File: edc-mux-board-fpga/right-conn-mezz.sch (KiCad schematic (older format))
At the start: 86 parts, among them J21 Device 10, J22 Device 13, J23 Device 11, J24 Device 14, J25 Left Mezzanine Board Connecto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, J26 Left Mezzanine Board Connecto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, J27 Device 12, J28 Device 15

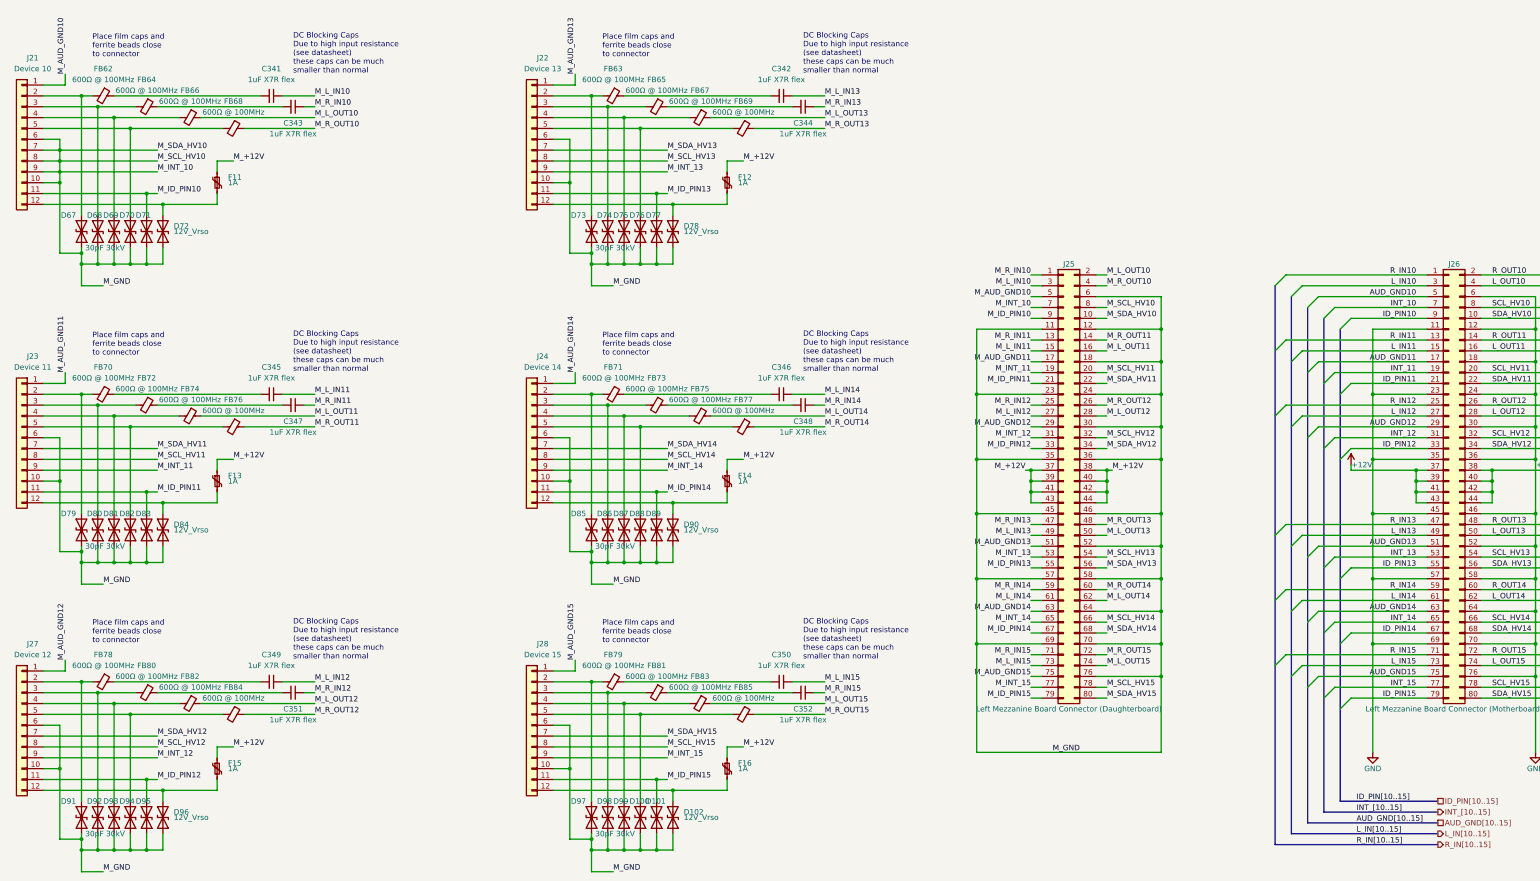
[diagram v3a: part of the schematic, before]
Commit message: re-annotating after adding power ICs and decoupling capacitors.
Also verified most footprints, and updated schematic field data.
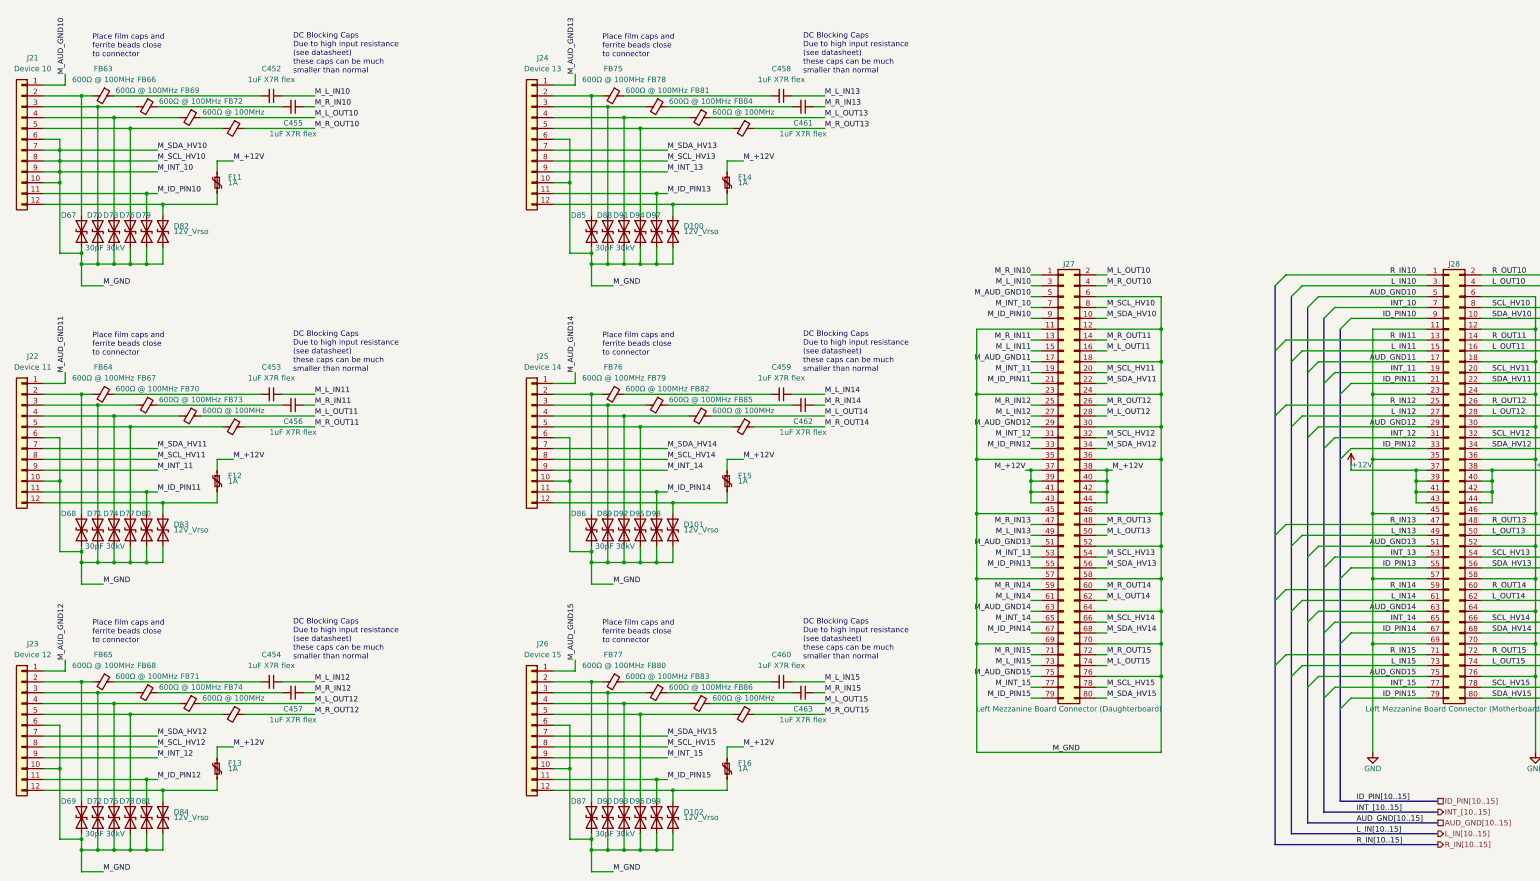
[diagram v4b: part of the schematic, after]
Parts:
- renumbered C341 to C452, C345 to C453, C349 to C454, C343 to C455, C347 to C456, C351 to C457, C342 to C458, C346 to C459, C350 to C460, C344 to C461, C348 to C462, C352 to C463, D78 to D100, D90 to D101, D79 to D68, D91 to D69, D68 to D70, D80 to D71, D92 to D72, D69 to D73, D81 to D74, D93 to D75, D70 to D76, D82 to D77, D94 to D78, D71 to D79, D83 to D80, D95 to D81, D72 to D82, D84 to D83, D96 to D84, D73 to D85, D85 to D86, D97 to D87, D74 to D88, D86 to D89, D98 to D90, D75 to D91, D87 to D92, D99 to D93, D76 to D94, D88 to D95, D100 to D96, D77 to D97, D89 to D98, D101 to D99, F13 to F12, F15 to F13, F12 to F14, F14 to F15, FB62 to FB63, FB70 to FB64, FB78 to FB65, FB64 to FB66, FB72 to FB67, FB80 to FB68, FB66 to FB69, FB74 to FB70, FB82 to FB71, FB68 to FB72, FB76 to FB73, FB84 to FB74, FB63 to FB75, FB71 to FB76, FB79 to FB77, FB65 to FB78, FB73 to FB79, FB81 to FB80, FB67 to FB81, FB75 to FB82, FB69 to FB84, FB77 to FB85, FB85 to FB86, J23 to J22, J27 to J23, J22 to J24, J24 to J25, J28 to J26, J25 to J27, J26 to J28

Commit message: removed polyfuses
at the right rating they were going to be too big.
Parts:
- removed F11, F12, F13, F14, F15, F16: 1A, Fuse:Fuse_0603_1608Metric, symbol Device:Polyfuse_Small
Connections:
- net M_+12V: now also D100.1 (A1), D101.1 (A1), D102.1 (A1), D82.1 (A1), D83.1 (A1), D84.1 (A1), J21.12 (Pin_12), J22.12 (Pin_12), J23.12 (Pin_12), J24.12 (Pin_12), J25.12 (Pin_12), J26.12 (Pin_12)
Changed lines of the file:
@@
 Wire Wire Line
 	1000 2600 2100 2600
-Wire Wire Line
-	2600 2600 2600 2500
 Text Label 2050 2100 0    50   ~ 0
 M_SDA_HV10
@@
 Text Label 2050 2500 0    50   ~ 0
 M_ID_PIN10
-$Comp
-L Device:Polyfuse_Small F?
-U 1 1 61B47DFE
-P 2600 2400
-AR Path="/5CC6CC1A/5CC6D47B/61B47DFE" Ref="F?"  Part="1"
-AR Path="/5CB02488/61B47DFE" Ref="F?"  Part="1"
-AR Path="/5CBF625C/61B47DFE" Ref="F?"  Part="1"
-AR Path="/5CBF628A/61B47DFE" Ref="F11"  Part="1"
-F 0 "F11" H 2700 2450 50  0000 L CNN
-F 1 "1A" H 2700 2400 50  0000 L CNN
-F 2 "Fuse:Fuse_0603_1608Metric" H 2650 2200 50  0001 L CNN
-F 3 "~" H 2600 2400 50  0001 C CNN
-F 4 "0603in/1608mm" H 400 -1600 50  0001 C CNN "Package ID"
-	1    2600 2400
-	1    0    0    -1
-$EndComp
 Wire Wire Line
 	2100 2600 2600 2600
-Wire Wire Line
-	2600 2300 2600 2200
 Text Label 1550 3350 0    50   ~ 0
 M_GND
@@
 Wire Wire Line
 	1000 5350 2100 5350
-Wire Wire Line
-	2600 5350 2600 5250
 Text Label 2050 4850 0    50   ~ 0
 M_SDA_HV11
@@
 Text Label 2050 5250 0    50   ~ 0
 M_ID_PIN11
-$Comp
-L Device:Polyfuse_Small F?
-U 1 1 61B47EDE
-P 2600 5150
-AR Path="/5CC6CC1A/5CC6D47B/61B47EDE" Ref="F?"  Part="1"
-AR Path="/5CB02488/61B47EDE" Ref="F?"  Part="1"
-AR Path="/5CBF625C/61B47EDE" Ref="F?"  Part="1"
-AR Path="/5CBF628A/61B47EDE" Ref="F12"  Part="1"
-F 0 "F12" H 2700 5200 50  0000 L CNN
-F 1 "1A" H 2700 5150 50  0000 L CNN
-F 2 "Fuse:Fuse_0603_1608Metric" H 2650 4950 50  0001 L CNN
-F 3 "~" H 2600 5150 50  0001 C CNN
-F 4 "0603in/1608mm" H 400 1150 50  0001 C CNN "Package ID"
-	1    2600 5150
-	1    0    0    -1
-$EndComp
 Wire Wire Line
 	2100 5350 2600 5350
-Wire Wire Line
-	2600 5050 2600 4950
 Text Label 1550 6100 0    50   ~ 0
 M_GND
@@
 Wire Wire Line
 	1000 8000 2100 8000
-Wire Wire Line
-	2600 8000 2600 7900
 Text Label 2050 7500 0    50   ~ 0
 M_SDA_HV12
@@
 Text Label 2050 7900 0    50   ~ 0
 M_ID_PIN12
-$Comp
-L Device:Polyfuse_Small F?
-U 1 1 61B47FAF
-P 2600 7800
-AR Path="/5CC6CC1A/5CC6D47B/61B47FAF" Ref="F?"  Part="1"
-AR Path="/5CB02488/61B47FAF" Ref="F?"  Part="1"
-AR Path="/5CBF625C/61B47FAF" Ref="F?"  Part="1"
-AR Path="/5CBF628A/61B47FAF" Ref="F13"  Part="1"
-F 0 "F13" H 2700 7850 50  0000 L CNN
-F 1 "1A" H 2700 7800 50  0000 L CNN
-F 2 "Fuse:Fuse_0603_1608Metric" H 2650 7600 50  0001 L CNN
-F 3 "~" H 2600 7800 50  0001 C CNN
-F 4 "0603in/1608mm" H 400 3800 50  0001 C CNN "Package ID"
-	1    2600 7800
-	1    0    0    -1
-$EndComp
 Wire Wire Line
 	2100 8000 2600 8000
-Wire Wire Line
-	2600 7700 2600 7600
 Text Label 1550 8750 0    50   ~ 0
 M_GND
@@
 Wire Wire Line
 	5700 2600 6800 2600
-Wire Wire Line
-	7300 2600 7300 2500
 Text Label 6750 2100 0    50   ~ 0
 M_SDA_HV13
@@
 Text Label 6750 2500 0    50   ~ 0
 M_ID_PIN13
-$Comp
-L Device:Polyfuse_Small F?
-U 1 1 61B48080
-P 7300 2400
-AR Path="/5CC6CC1A/5CC6D47B/61B48080" Ref="F?"  Part="1"
-AR Path="/5CB02488/61B48080" Ref="F?"  Part="1"
-AR Path="/5CBF625C/61B48080" Ref="F?"  Part="1"
-AR Path="/5CBF628A/61B48080" Ref="F14"  Part="1"
-F 0 "F14" H 7400 2450 50  0000 L CNN
-F 1 "1A" H 7400 2400 50  0000 L CNN
-F 2 "Fuse:Fuse_0603_1608Metric" H 7350 2200 50  0001 L CNN
-F 3 "~" H 7300 2400 50  0001 C CNN
-F 4 "0603in/1608mm" H 5100 -1600 50  0001 C CNN "Package ID"
-	1    7300 2400
-	1    0    0    -1
-$EndComp
 Wire Wire Line
 	6800 2600 7300 2600
-Wire Wire Line
-	7300 2300 7300 2200
 Text Label 6250 3350 0    50   ~ 0
 M_GND
@@
 Wire Wire Line
 	5700 5350 6800 5350
-Wire Wire Line
-	7300 5350 7300 5250
 Text Label 6750 4850 0    50   ~ 0
 M_SDA_HV14
@@
 Text Label 6750 5250 0    50   ~ 0
 M_ID_PIN14
-$Comp
-L Device:Polyfuse_Small F?
-U 1 1 61B48151
-P 7300 5150
-AR Path="/5CC6CC1A/5CC6D47B/61B48151" Ref="F?"  Part="1"
-AR Path="/5CB02488/61B48151" Ref="F?"  Part="1"
-AR Path="/5CBF625C/61B48151" Ref="F?"  Part="1"
-AR Path="/5CBF628A/61B48151" Ref="F15"  Part="1"
-F 0 "F15" H 7400 5200 50  0000 L CNN
-F 1 "1A" H 7400 5150 50  0000 L CNN
-F 2 "Fuse:Fuse_0603_1608Metric" H 7350 4950 50  0001 L CNN
-F 3 "~" H 7300 5150 50  0001 C CNN
-F 4 "0603in/1608mm" H 5100 1150 50  0001 C CNN "Package ID"
-	1    7300 5150
-	1    0    0    -1
-$EndComp
 Wire Wire Line
 	6800 5350 7300 5350
-Wire Wire Line
-	7300 5050 7300 4950
 Text Label 6250 6100 0    50   ~ 0
 M_GND
@@
 Wire Wire Line
 	5700 8000 6800 8000
-Wire Wire Line
-	7300 8000 7300 7900
 Text Label 6750 7500 0    50   ~ 0
 M_SDA_HV15
@@
 Text Label 6750 7900 0    50   ~ 0
 M_ID_PIN15
-$Comp
-L Device:Polyfuse_Small F?
-U 1 1 61B48222
-P 7300 7800
-AR Path="/5CC6CC1A/5CC6D47B/61B48222" Ref="F?"  Part="1"
-AR Path="/5CB02488/61B48222" Ref="F?"  Part="1"
-AR Path="/5CBF625C/61B48222" Ref="F?"  Part="1"
-AR Path="/5CBF628A/61B48222" Ref="F16"  Part="1"
-F 0 "F16" H 7400 7850 50  0000 L CNN
-F 1 "1A" H 7400 7800 50  0000 L CNN
-F 2 "Fuse:Fuse_0603_1608Metric" H 7350 7600 50  0001 L CNN
-F 3 "~" H 7300 7800 50  0001 C CNN
-F 4 "0603in/1608mm" H 5100 3800 50  0001 C CNN "Package ID"
-	1    7300 7800
-	1    0    0    -1
-$EndComp
 Wire Wire Line
 	6800 8000 7300 8000
-Wire Wire Line
-	7300 7700 7300 7600
 Text Label 6250 8750 0    50   ~ 0
 M_GND
@@
 Wire Wire Line
 	1150 2300 1150 2400
+Wire Wire Line
+	2600 2200 2600 2600
+Wire Wire Line
+	2600 4950 2600 5350
+Wire Wire Line
+	2600 7600 2600 8000
+Wire Wire Line
+	7300 7600 7300 8000
+Wire Wire Line
+	7300 4950 7300 5350
+Wire Wire Line
+	7300 2200 7300 2600
 Wire Bus Line
 	12350 3350 12350 8500

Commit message: Reannotating and adding more fields to components
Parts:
- C454: renamed from C452; Characteristics (none) -> CAP CER 0805 1UF 25V X7R 5%; Description (none) -> MLCC Capacitor; Manufacturers Part Number C0805X105J3RACAUTO -> C0805X105J3RECAUTO
- C455: renamed from C453; Characteristics (none) -> CAP CER 0805 1UF 25V X7R 5%; Description (none) -> MLCC Capacitor; Manufacturers Part Number C0805X105J3RACAUTO -> C0805X105J3RECAUTO
- C456: renamed from C454; Characteristics (none) -> CAP CER 0805 1UF 25V X7R 5%; Description (none) -> MLCC Capacitor; Manufacturers Part Number C0805X105J3RACAUTO -> C0805X105J3RECAUTO
- C457: renamed from C455; Characteristics (none) -> CAP CER 0805 1UF 25V X7R 5%; Description (none) -> MLCC Capacitor; Manufacturers Part Number C0805X105J3RACAUTO -> C0805X105J3RECAUTO
- C458: renamed from C456; Characteristics (none) -> CAP CER 0805 1UF 25V X7R 5%; Description (none) -> MLCC Capacitor; Manufacturers Part Number C0805X105J3RACAUTO -> C0805X105J3RECAUTO
- C459: renamed from C457; Characteristics (none) -> CAP CER 0805 1UF 25V X7R 5%; Description (none) -> MLCC Capacitor; Manufacturers Part Number C0805X105J3RACAUTO -> C0805X105J3RECAUTO
- C460: renamed from C458; Characteristics (none) -> CAP CER 0805 1UF 25V X7R 5%; Description (none) -> MLCC Capacitor; Manufacturers Part Number C0805X105J3RACAUTO -> C0805X105J3RECAUTO
- C461: renamed from C459; Characteristics (none) -> CAP CER 0805 1UF 25V X7R 5%; Description (none) -> MLCC Capacitor; Manufacturers Part Number C0805X105J3RACAUTO -> C0805X105J3RECAUTO
- C462: renamed from C460; Characteristics (none) -> CAP CER 0805 1UF 25V X7R 5%; Description (none) -> MLCC Capacitor; Manufacturers Part Number C0805X105J3RACAUTO -> C0805X105J3RECAUTO
- C463: renamed from C461; Characteristics (none) -> CAP CER 0805 1UF 25V X7R 5%; Description (none) -> MLCC Capacitor; Manufacturers Part Number C0805X105J3RACAUTO -> C0805X105J3RECAUTO
- C464: renamed from C462; Characteristics (none) -> CAP CER 0805 1UF 25V X7R 5%; Description (none) -> MLCC Capacitor; Manufacturers Part Number C0805X105J3RACAUTO -> C0805X105J3RECAUTO
- C465: renamed from C463; Characteristics (none) -> CAP CER 0805 1UF 25V X7R 5%; Description (none) -> MLCC Capacitor; Manufacturers Part Number C0805X105J3RACAUTO -> C0805X105J3RECAUTO
- FB63, FB64, FB65, FB66, FB67, FB68, FB69, FB70, FB71, FB72, FB73, FB74, FB75, FB76, FB77, FB78, FB79, FB80, FB81, FB82, FB83, FB84, FB85, FB86: footprint Capacitor_SMD:C_0805_2012Metric -> Inductor_SMD:L_0805_2012Metric; Characteristics (none) -> 600 Ohms @ 100MHz 1 Signal Line Ferrite Bead 0805 (2012 Met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; Description (none) -> Ferrite Bead; Manufacturers Part Number BLM21AG601BH1 -> BLM21AG601SZ1D
- J21, J22, J23, J24, J25, J26: Description (none) -> M12 A Coded 12 Pin Connector; Package ID (none) -> Through Hole
- J27, J28: Package ID (none) -> Through Hole

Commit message: Fixed pin header footprint issues
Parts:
- J27: footprint Connector_PinSocket_2.54mm:PinSocket_2x10_P2.54mm_Horizontal -> Connector_PinSocket_2.54mm:PinSocket_2x40_P2.54mm_Horizontal
- J28: footprint Connector_PinHeader_2.54mm:PinHeader_2x10_P2.54mm_Vertical -> Connector_PinHeader_2.54mm:PinHeader_2x40_P2.54mm_Vertical
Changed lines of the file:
@@
 F 0 "J27" H 10450 7150 50  0000 C CNN
 F 1 "Left Mezzanine Board Connector (Daughterboard)" H 10450 3050 50  0000 C CNN
-F 2 "Connector_PinSocket_2.54mm:PinSocket_2x10_P2.54mm_Horizontal" H 10400 5150 50  0001 C CNN
+F 2 "Connector_PinSocket_2.54mm:PinSocket_2x40_P2.54mm_Horizontal" H 10400 5150 50  0001 C CNN
 F 3 "~" H 10400 5150 50  0001 C CNN
 F 4 "Through Hole" H 0   0   50  0001 C CNN "Package ID"
@@
 F 0 "J28" H 14000 7150 50  0000 C CNN
 F 1 "Left Mezzanine Board Connector (Motherboard)" H 14000 3050 50  0000 C CNN
-F 2 "Connector_PinHeader_2.54mm:PinHeader_2x10_P2.54mm_Vertical" H 13950 5150 50  0001 C CNN
+F 2 "Connector_PinHeader_2.54mm:PinHeader_2x40_P2.54mm_Vertical" H 13950 5150 50  0001 C CNN
 F 3 "~" H 13950 5150 50  0001 C CNN
 F 4 "Through Hole" H 0   0   50  0001 C CNN "Package ID"

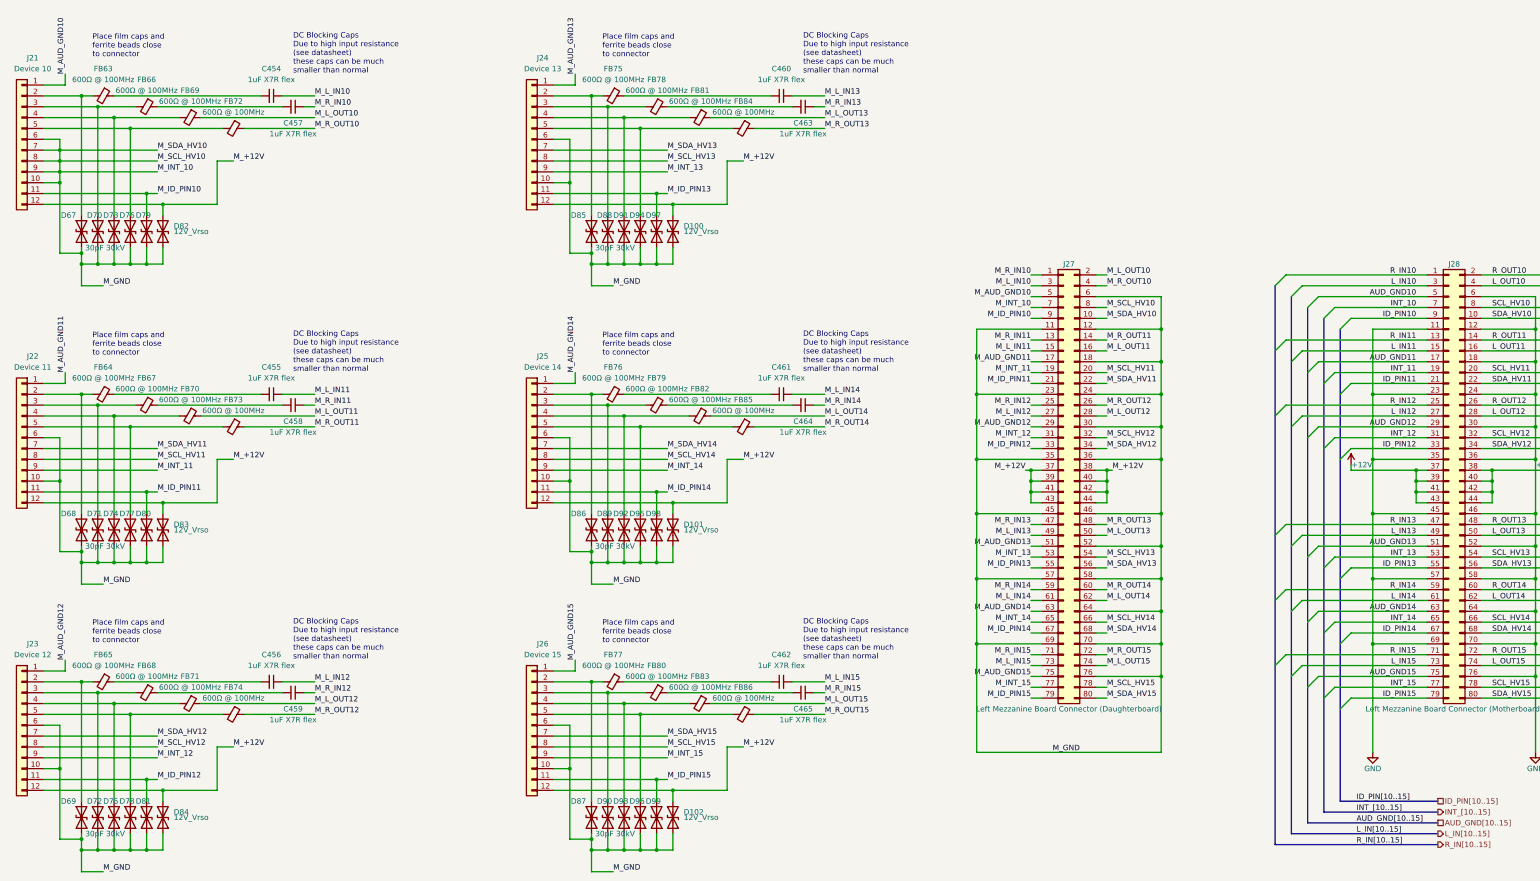
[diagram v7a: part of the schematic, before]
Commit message: Reannotating board
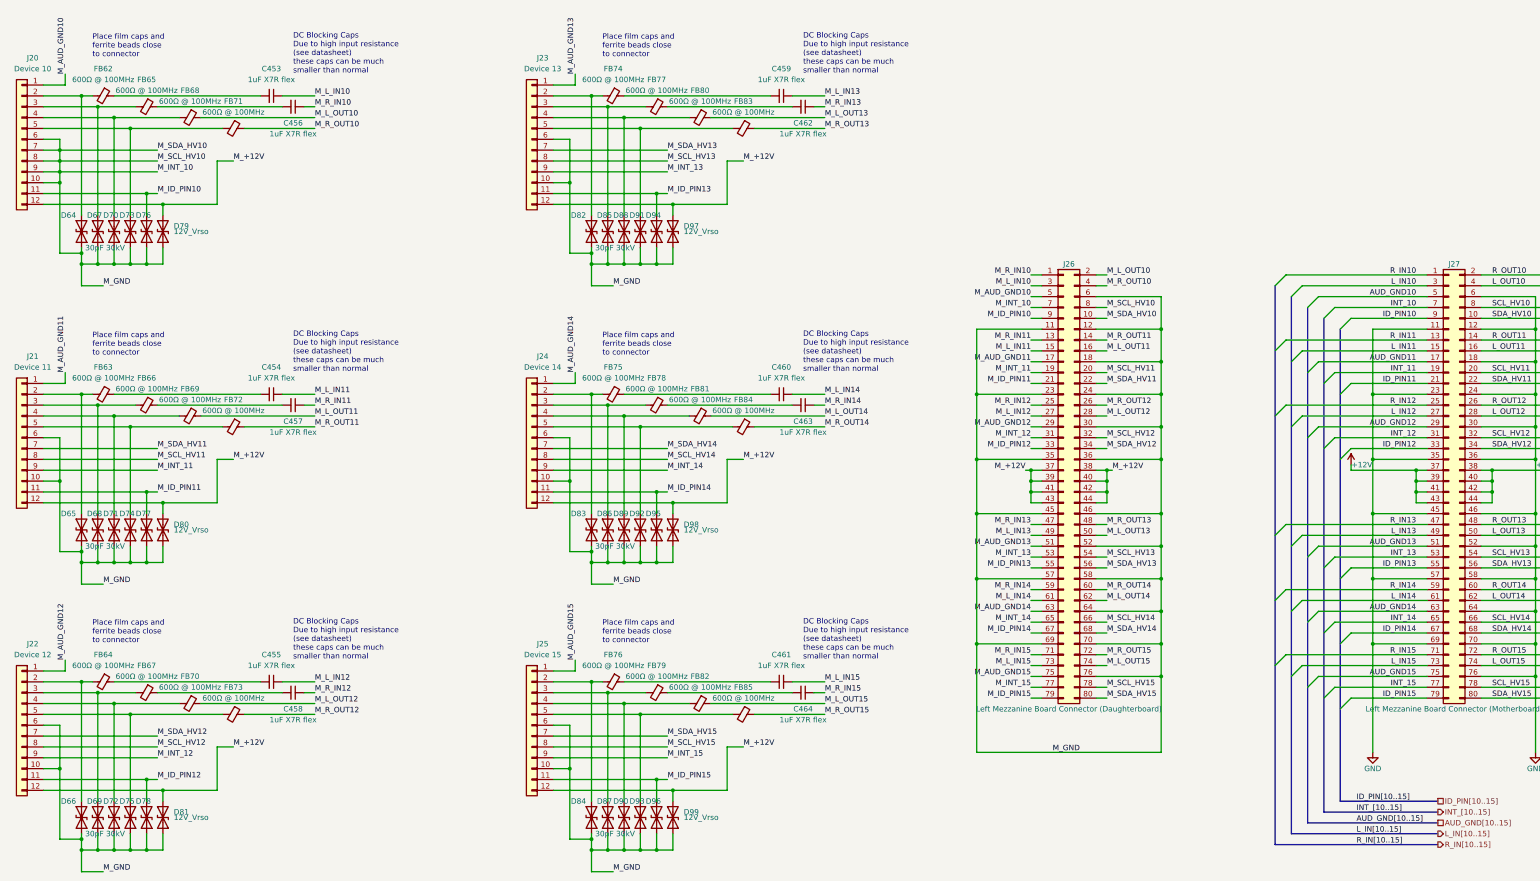
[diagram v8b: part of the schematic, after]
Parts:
- renumbered C454 to C453, C455 to C454, C456 to C455, C457 to C456, C458 to C457, C459 to C458, C460 to C459, C461 to C460, C462 to C461, C463 to C462, C464 to C463, C465 to C464, D67 to D64, D68 to D65, D69 to D66, D70 to D67, D71 to D68, D72 to D69, D73 to D70, D74 to D71, D75 to D72, D76 to D73, D77 to D74, D78 to D75, D79 to D76, D80 to D77, D81 to D78, D82 to D79, D83 to D80, D84 to D81, D85 to D82, D86 to D83, D87 to D84, D88 to D85, D89 to D86, D90 to D87, D91 to D88, D92 to D89, D93 to D90, D94 to D91, D95 to D92, D96 to D93, D97 to D94, D98 to D95, D99 to D96, D100 to D97, D101 to D98, D102 to D99, FB63 to FB62, FB64 to FB63, FB65 to FB64, FB66 to FB65, FB67 to FB66, FB68 to FB67, FB69 to FB68, FB70 to FB69, FB71 to FB70, FB72 to FB71, FB73 to FB72, FB74 to FB73, FB75 to FB74, FB76 to FB75, FB77 to FB76, FB78 to FB77, FB79 to FB78, FB80 to FB79, FB81 to FB80, FB82 to FB81, FB83 to FB82, FB84 to FB83, FB85 to FB84, FB86 to FB85, J21 to J20, J22 to J21, J23 to J22, J24 to J23, J25 to J24, J26 to J25, J27 to J26, J28 to J27
